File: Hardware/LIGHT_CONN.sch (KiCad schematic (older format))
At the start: 73 parts, among them P10 AI_RGB, P11 AI_RGB, P12 AI_RGB, P13 AI_RGB, P14 CONN_01X04, P15 AI_RGB, P16 AI_RGB, P17 AI_RGB, P18 AI_RGB, P19 AI_RGB, P2 AI_RGB, P20 CONN_01X04, P21 AI_RGB, P3 CONN_01X04, P4 AI_RGB, P5 AI_RGB, P6 AI_RGB, P7 AI_RGB, P8 AI_RGB, P9 CONN_01X04, Q10 MOSFET_N, Q11 MOSFET_N, Q12 MOSFET_N, Q13 MOSFET_N, Q2 MOSFET_N, Q3 MOSFET_N, Q4 MOSFET_N, Q5 MOSFET_N, Q6 MOSFET_N, Q7 MOSFET_N, Q8 MOSFET_N, Q9 MOSFET_N, U10 PCA9685BS

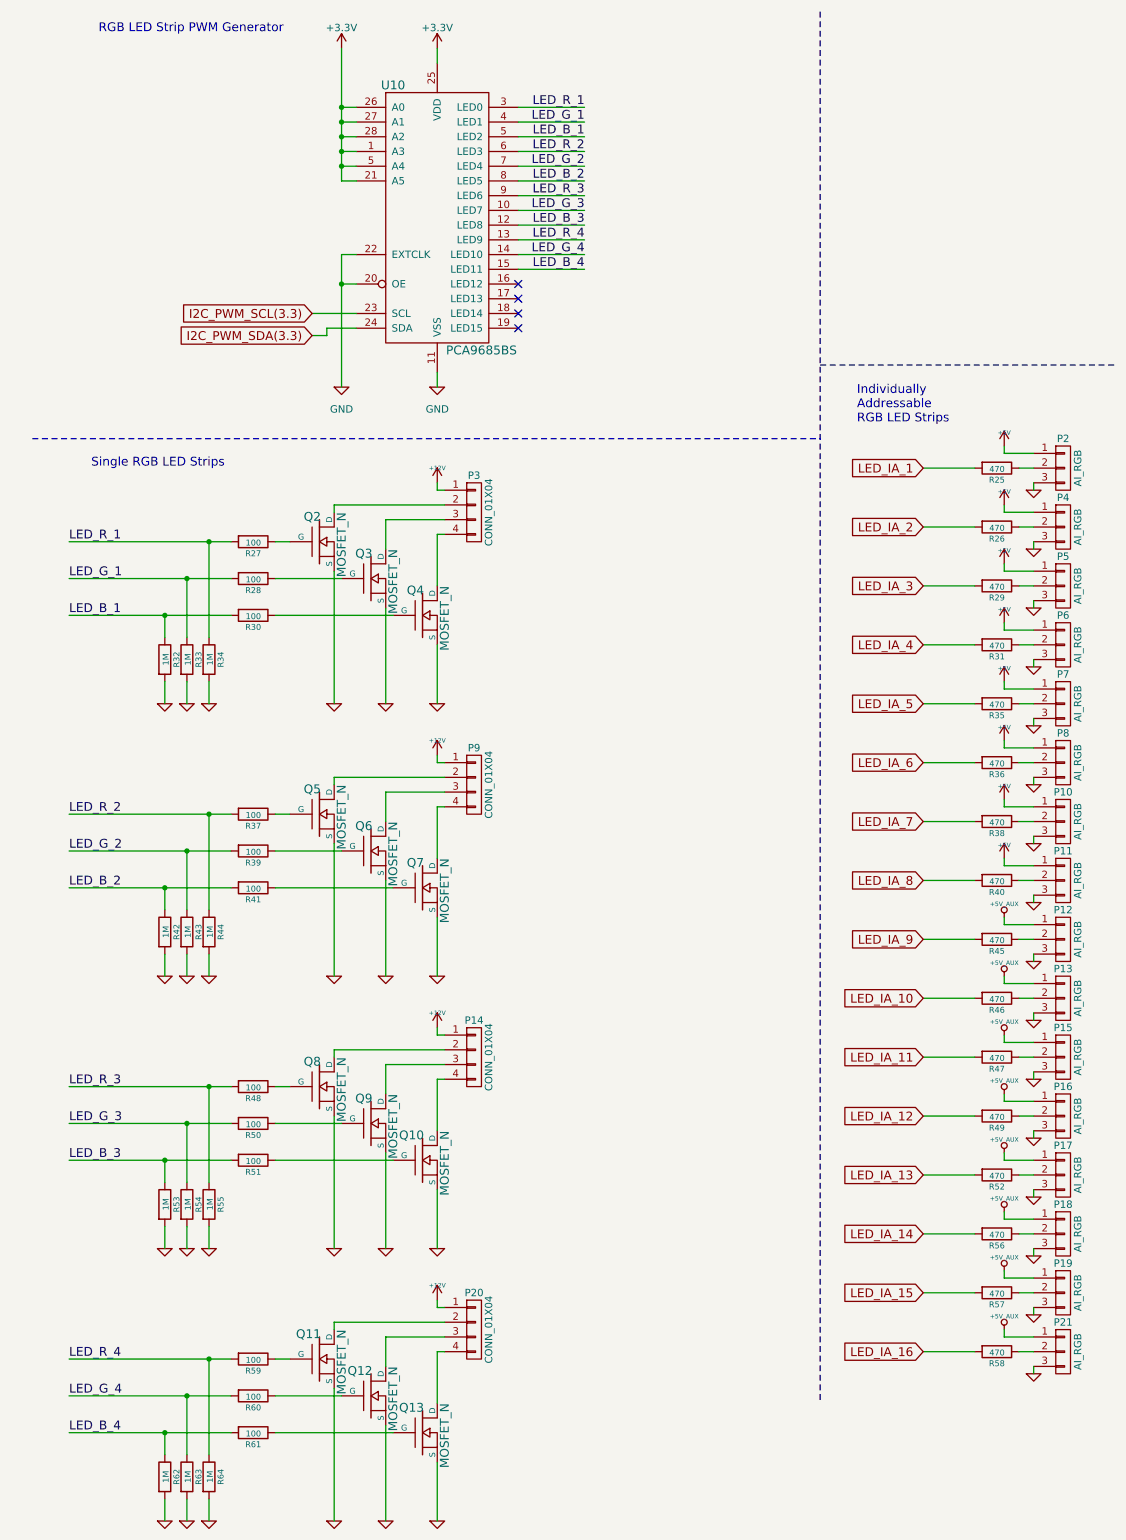
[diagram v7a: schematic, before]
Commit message: Made design review fixes, added breakouts
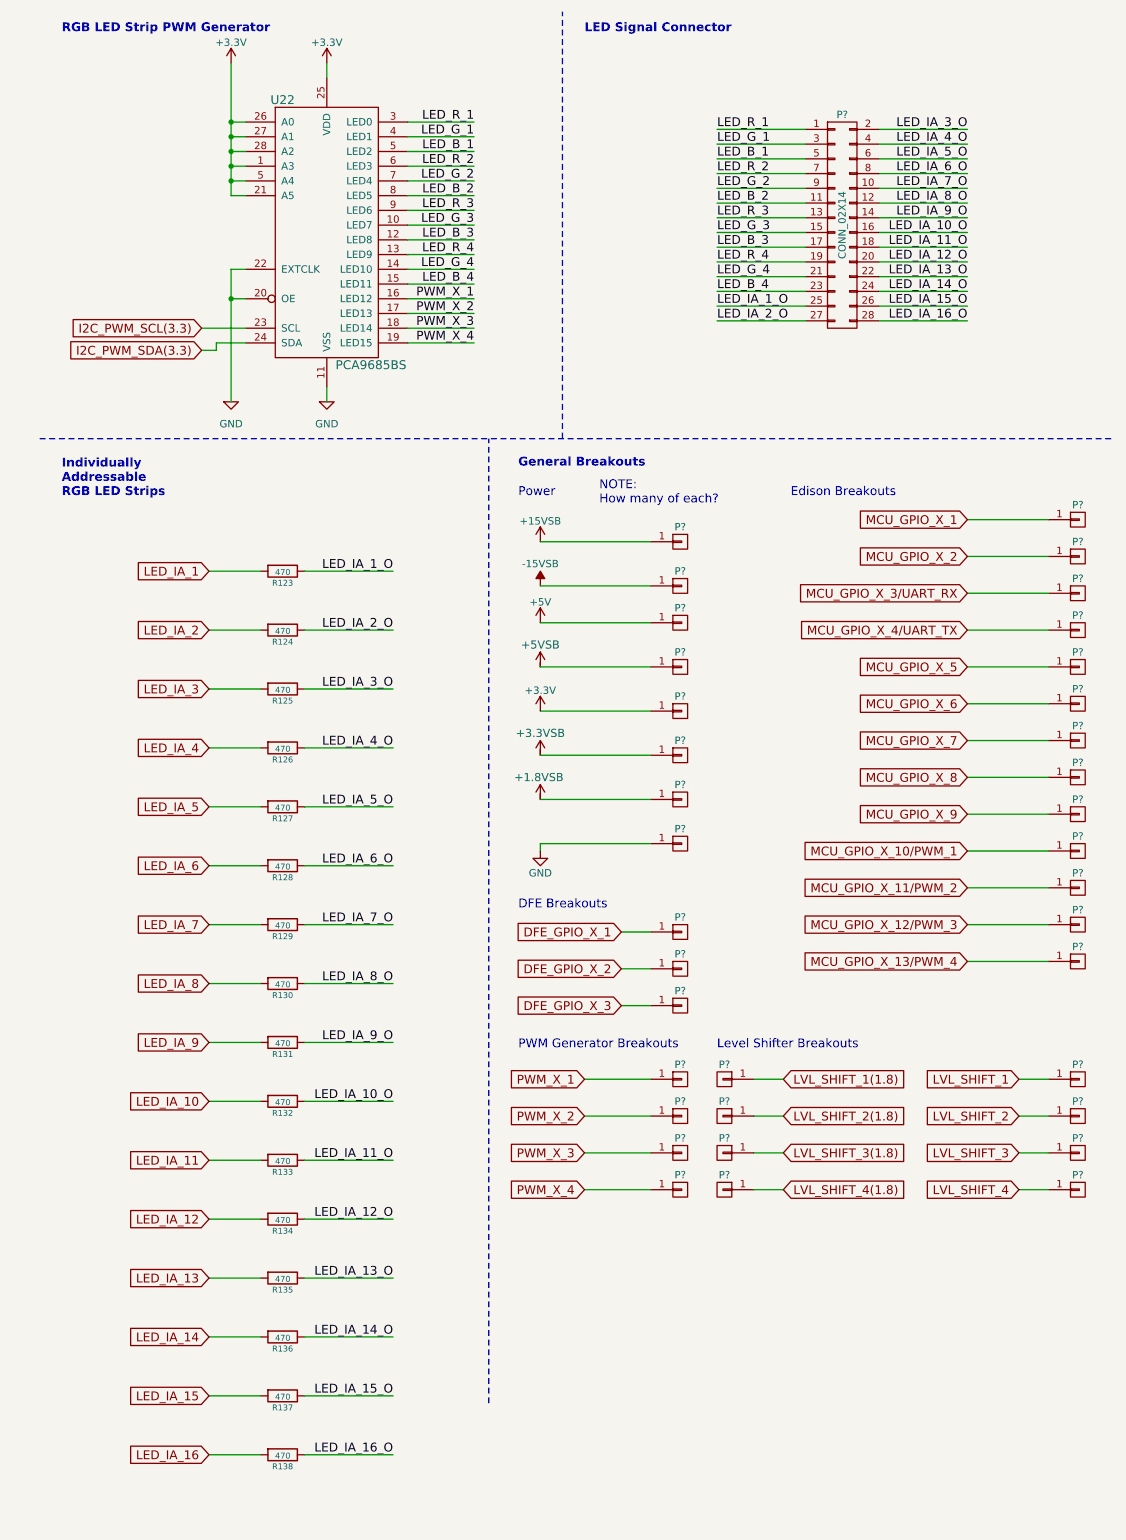
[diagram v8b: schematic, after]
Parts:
- removed P10, P11, P12, P13, P15, P16, P17, P18, P19, P2, P21, P4, P5, P6, P7, P8: AI_RGB, symbol CONN_01X03
- removed P14, P20, P3, P9: CONN_01X04, symbol CONN_01X04
- removed Q10, Q11, Q12, Q13, Q2, Q3, Q4, Q5, Q6, Q7, Q8, Q9: MOSFET_N, symbol MOSFET_N
- removed R27, R28, R30, R37, R39, R41, R48, R50, R51, R59, R60, R61: 100, symbol R-RESCUE-museV2
- removed R32, R33, R34, R42, R43, R44, R53, R54, R55, R62, R63, R64: 1M, symbol R-RESCUE-museV2
- added P?: CONN_02X14, symbol CONN_02X14
- added P? (x36): CONN_01X01, symbol CONN_01X01
- renumbered R25 to R123, R26 to R124, R29 to R125, R31 to R126, R35 to R127, R36 to R128, R38 to R129, R40 to R130, R45 to R131, R46 to R132, R47 to R133, R49 to R134, R52 to R135, R56 to R136, R57 to R137, R58 to R138, U10 to U22
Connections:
- net +3V3: now also P?.1 (P1)
- net +5V: now also P?.1 (P1)
- net GND: now also P?.1 (P1)
- net LED_B_1: now also P?.5 (P5)
- net LED_B_2: now also P?.11 (P11)
- net LED_B_3: now also P?.17 (P17)
- net LED_B_4: now also P?.23 (P23)
- net LED_G_1: now also P?.3 (P3)
- net LED_G_2: now also P?.9 (P9)
- net LED_G_3: now also P?.15 (P15)
- net LED_G_4: now also P?.21 (P21)
- net LED_R_1: now also P?.1 (P1)
- net LED_R_2: now also P?.7 (P7)
- net LED_R_3: now also P?.13 (P13)
- net LED_R_4: now also P?.19 (P19)
- net LED_IA_1_O: now reaches R123.1
- net LED_IA_1_O: now also P?.25 (P25)
- net LED_IA_2_O: now reaches R124.1
- net LED_IA_2_O: now also P?.27 (P27)
- net LED_IA_3_O: now reaches R125.1
- net LED_IA_3_O: now also P?.2 (P2)
- net LED_IA_4_O: now reaches R126.1
- net LED_IA_4_O: now also P?.4 (P4)
- net LED_IA_5_O: now reaches R127.1
- net LED_IA_5_O: now also P?.6 (P6)
- net LED_IA_6_O: now reaches R128.1
- net LED_IA_6_O: now also P?.8 (P8)
- net LED_IA_7_O: now reaches R129.1
- net LED_IA_7_O: now also P?.10 (P10)
- net LED_IA_8_O: now reaches R130.1
- net LED_IA_8_O: now also P?.12 (P12)
- net LED_IA_9_O: now reaches R131.1
- net LED_IA_9_O: now also P?.14 (P14)
- net LED_IA_10_O: now reaches R132.1
- net LED_IA_10_O: now also P?.16 (P16)
- net LED_IA_11_O: now reaches R133.1
- net LED_IA_11_O: now also P?.18 (P18)
- net LED_IA_12_O: now reaches R134.1
- net LED_IA_12_O: now also P?.20 (P20)
- net LED_IA_13_O: now reaches R135.1
- net LED_IA_13_O: now also P?.22 (P22)
- net LED_IA_14_O: now reaches R136.1
- net LED_IA_14_O: now also P?.24 (P24)
- net LED_IA_15_O: now reaches R137.1
- net LED_IA_15_O: now also P?.26 (P26)
- net LED_IA_16_O: now reaches R138.1
- net LED_IA_16_O: now also P?.28 (P28)
- net PWM_X_1: now reaches U22.16 (LED12)
- net PWM_X_1: now also P?.1 (P1)
- net PWM_X_2: now reaches U22.17 (LED13)
- net PWM_X_2: now also P?.1 (P1)
- net PWM_X_3: now reaches U22.18 (LED14)
- net PWM_X_3: now also P?.1 (P1)
- net PWM_X_4: now reaches U22.19 (LED15)
- net PWM_X_4: now also P?.1 (P1)
- new net +1.8VSB: P?.1 (P1)
- new net +15V: P?.1 (P1)
- new net +3.3VSB: P?.1 (P1)
- new net +5VSB: P?.1 (P1)
- new net -15V: P?.1 (P1)
- new net DFE_GPIO_X_1: P?.1 (P1)
- new net DFE_GPIO_X_2: P?.1 (P1)
- new net DFE_GPIO_X_3: P?.1 (P1)
- new net LVL_SHIFT_1: P?.1 (P1)
- new net LVL_SHIFT_1(1.8): P?.1 (P1)
- new net LVL_SHIFT_2: P?.1 (P1)
- new net LVL_SHIFT_2(1.8): P?.1 (P1)
- new net LVL_SHIFT_3: P?.1 (P1)
- new net LVL_SHIFT_3(1.8): P?.1 (P1)
- new net LVL_SHIFT_4: P?.1 (P1)
- new net LVL_SHIFT_4(1.8): P?.1 (P1)
- new net MCU_GPIO_X_1: P?.1 (P1)
- new net MCU_GPIO_X_10/PWM_1: P?.1 (P1)
- new net MCU_GPIO_X_11/PWM_2: P?.1 (P1)
- new net MCU_GPIO_X_12/PWM_3: P?.1 (P1)
- new net MCU_GPIO_X_13/PWM_4: P?.1 (P1)
- new net MCU_GPIO_X_2: P?.1 (P1)
- new net MCU_GPIO_X_3/UART_RX: P?.1 (P1)
- new net MCU_GPIO_X_4/UART_TX: P?.1 (P1)
- new net MCU_GPIO_X_5: P?.1 (P1)
- new net MCU_GPIO_X_6: P?.1 (P1)
- new net MCU_GPIO_X_7: P?.1 (P1)
- new net MCU_GPIO_X_8: P?.1 (P1)
- new net MCU_GPIO_X_9: P?.1 (P1)
- no-connect marks 4 -> 0
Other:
- note added: "DFE Breakouts"
- note added: "Edison Breakouts"
- note added: "General Breakouts"
- note added: "LED Signal Connector"
- note added: "Level Shifter Breakouts"
- note added: "NOTE:\nHow many of each?"
- note added: "PWM Generator Breakouts"
- note added: "Power"
- note removed: "Single RGB LED Strips"
- moved on the sheet: R123, R124, R125, R126, R127, R128, R129, R130, R131, R132, R133, R134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
